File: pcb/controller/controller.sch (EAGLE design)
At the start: 86 parts, among them J1 DL-2MM-HEADER-14, J10 SNG-100-HEADER-03-HDR-V, J2 DL-1.25MM-HEADER-20, J3 MICRO_SD, J4 SNG-2MM-HEADER-03-SMT-V, J5 7498011122R, J6 USB_A, J7 SNG-2MM-HEADER-09-V, J8 CUI-PJ-013C, J9 SNG-100-HEADER-04-HDR-V, Q1 12MHz, U1 LM3526M-L, U2 ARIA_G25, U3 PCM2704C, U4 TPA2005D1DGN, U5 ADP2303ARDZ, U6 TPS62086RLT, U7 TS4040D30IDBZ

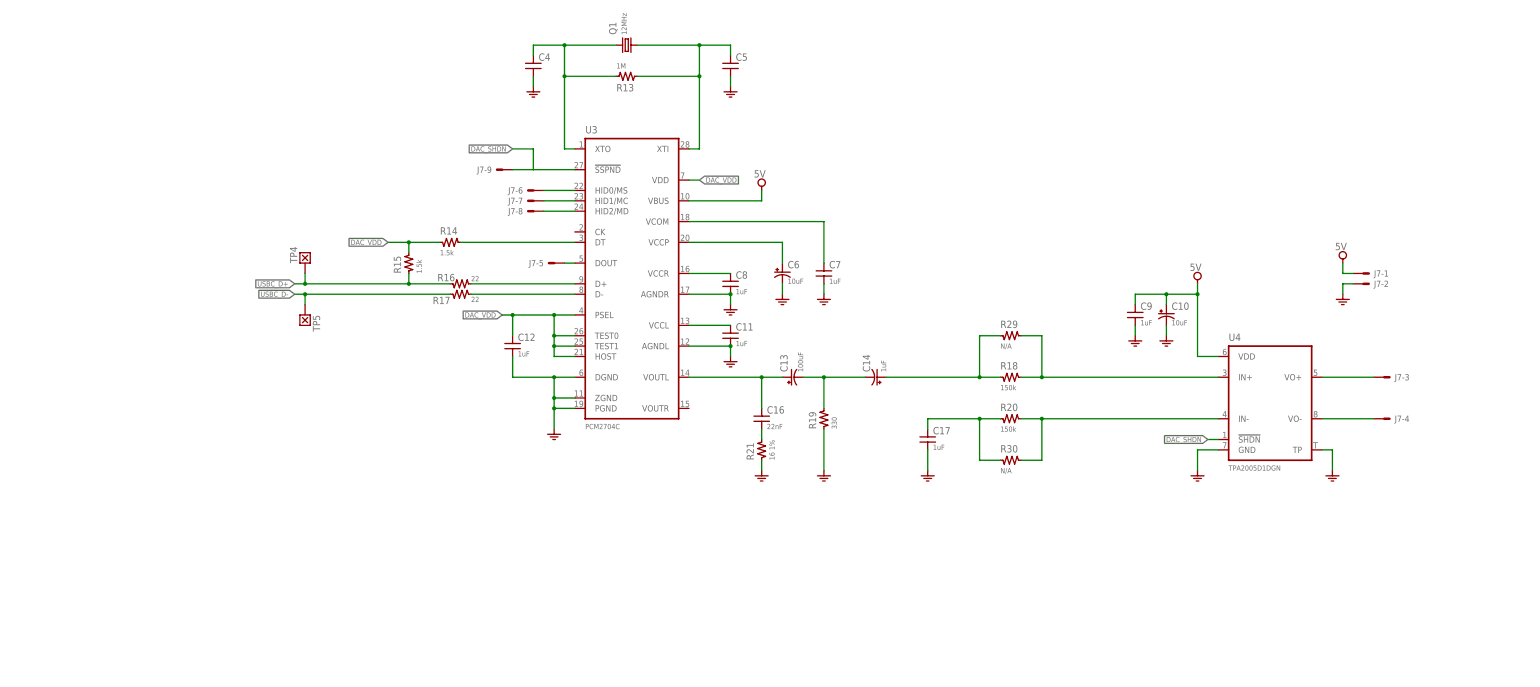
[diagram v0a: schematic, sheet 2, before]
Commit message: Corrected drawings of touch panel PCB
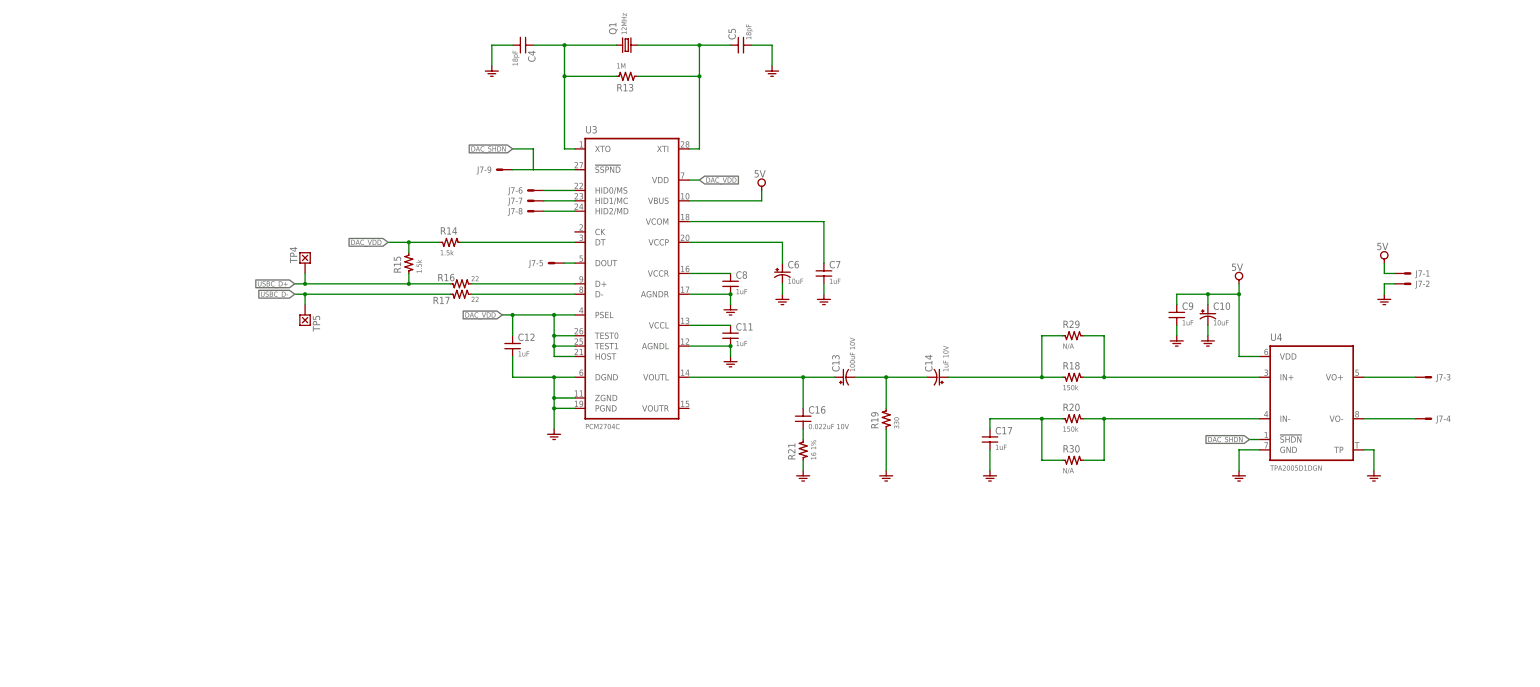
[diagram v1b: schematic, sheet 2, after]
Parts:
- removed R22, R27: 100k, Passive:RES-0603
- removed R23: 53.6K 1%, Passive:RES-0603
- removed R25: 10K 1%, Passive:RES-0603
- added C15: 10uF 10v, Passive:CAP-1206
- added C27: 22uF 6.3V, Passive:CAP-1206
- added C28: 47uF 6.3v, Passive:CAP-1206
- added D2: 30V 4A, Passive:DIODE-DO214-AA
- C13: value 100uF -> 100uF 10V
- C14: value 1uF -> 1uF 10V
- C16: value 22nF -> 0.022uF 10V
- C18, C19: value 10uF 50V -> 10uF 25V; device Passive:CAP-0805 -> Passive:CAP-1206; DESCRIPTION {DESCRIPTION} - SMT 0805 - {value} -> {DESCRIPTION} - SMT 1206 - {value}; PACKAGE SMT 0805 -> SMT 1206
- C21: value 100nF -> 100nF 25v
- C22: value 10uF 50v -> 10uF 25v
- C23: value 100uF -> 22uF 6.3V
- C24: value (none) -> 100nF; device Passive:CAP-1206 -> Passive:CAP-0603
- C25: value (none) -> 47uF 6.3v
- C26: value (none) -> 100nF
- C4, C5: value (none) -> 18pF
- D1: value 40V 3A -> 30V 4A
- L4: value (none) -> 10uH; device Passive:IND-74437324022 -> Passive:IND-10X10; MFG (none) -> TDK; PART_NO (none) -> CLF10040T-100M
- L5: value (none) -> 4.7uH; device Passive:IND-MPI4040R2-R47-R -> Passive:IND-10X10; PART_NO (none) -> CLF10040T-4R7N
- TP1, TP2: device Misc:TEST_POINT-050 -> Misc:WIRE
- U5: value ADP2303ARDZ -> ADP2302ARDZ-5.0; device Power:ADP2303ARDZ -> Power:ADP2302ARDZ-5.0; DESCRIPTION (none) -> {DESCRIPTION} - 2A, 5V
- U6: value TPS62086RLT -> ADP2303ARDZ-3.3; device Power:TPS62086RLT -> Power:ADP2303ARDZ-3.3; DESCRIPTION (none) -> {DESCRIPTION} - 3A, 3.3v
- U7: value TS4040D30IDBZ -> LM4040D25IDBZR; PART_NO (none) -> LM4040D25IDBZR
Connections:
- net N$2 renamed IN_GND
- removed net N$3: R22.2, U5.PGOOD
- removed net N$34: R23.1, R25.2, U5.FB
- removed net N$35: L5.P$1, U6.SW
- new net N$10: C24.2, D2.K, L5.1, U6.SW
- net 3.3V: now also C28.1, L5.2; no longer L5.P$2, R27.2, U6.VOS
- net 5V: now also C27.1, L4.2, U5.FB; no longer C24.1, L4.P$2, R23.2, U6.EN, U6.VIN
- net GND: now also C15.2, C27.2, C28.2, D2.A, U6.EPAD, U6.GND; no longer C24.2, R25.1
- net N$33: now also L4.1; no longer L4.P$1
- net N$36: now also C24.1, U6.BST; no longer R27.1, U6.PG
- net VCC: now also C15.1, J9-1.S, U6.EN, U6.VIN; no longer J9-2.S, R22.1
- net V_MAIN: now also J9-2.S; no longer J9-1.S
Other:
- note added: "3.3V STEP DOWN DC-DC"
- moved on the sheet: C10, C13, C14, C16, C17, C22, C23, C24, C25, C4, C5, C9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

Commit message: Display base pcb (rev C), Touch panel (rev B)
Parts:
- removed J10: SNG-100-HEADER-03-HDR-V, Connectors:SNG-100-HEADER-03-HDR-V
- removed R17: 22, Passive:RES-0603
- removed TP3: (no value), Misc:TEST_POINT-TP_75X75
- removed TP4, TP5: (no value), Misc:TEST_POINT-050
- added C29: 1uF, Passive:CAP-0603
- added C30: 22uF (10v), Passive:CAP-E-1206-TANT
- added C31: 47uF (6.3v), Passive:CAP-E-1206-TANT
- added C32, C33: N/A, Passive:CAP-0603
- added L6, L7: 0, Passive:IND-0603
- added R22, R23: 1 (1%), Passive:RES-0805
- added U8: CAT811TTBI, IC:CAT811TTBI
- added W1: (no value), Misc:WIRE-150X75
- added W2: DRX, Misc:WIRE-150X75
- added W3: DTX, Misc:WIRE-150X75
- added W4: GND, Misc:WIRE-150X75
- C10, C14, C6: device Passive:CAP-E-S0805 -> Passive:CAP-E-0805-ALUM; DESCRIPTION (none) -> Aluminium capacitor - SMT 0805 - {VALUE}
- C13: device Passive:CAP-E-S1210 -> Passive:CAP-E-1210-ALUM; DESCRIPTION (none) -> Aluminium capacitor - SMT 1210 - {VALUE}; MFG (none) -> AVX
- C15: value 10uF 10v -> 10uF (25v); device Passive:CAP-1206 -> Passive:CAP-E-1210-TANT; DESCRIPTION {DESCRIPTION} - SMT 1206 - {value} -> (none); MFG (none) -> AVX; PACKAGE SMT 1206 -> (none); PART_NO (none) -> TPSB106K025R1800
- C21: value 100nF 25v -> 100nF 25V
- C22: value 10uF 25v -> 10uF (25v); device Passive:CAP-1206 -> Passive:CAP-E-1210-TANT; DESCRIPTION {DESCRIPTION} - SMT 1206 - {value} -> (none); MFG (none) -> AVX; PACKAGE SMT 1206 -> (none); PART_NO (none) -> TPSB106K025R1800
- C23: value 22uF 6.3V -> 22uF (10v); device Passive:CAP-1206 -> Passive:CAP-E-1206-TANT; DESCRIPTION (none) -> Tantalum capacitor - SMT 1206 - {VALUE}; MFG (none) -> AVX; PART_NO (none) -> TPSA226M010R0900
- C24: value 100nF -> 100nF 25V
- C25: value 47uF 6.3v -> 47uF (6.3v); device Passive:CAP-1206 -> Passive:CAP-E-1206-TANT; DESCRIPTION (none) -> Tantalum capacitor - SMT 1206 - {VALUE}; MFG (none) -> AVX; PART_NO (none) -> TPSA476K006R0800
- C27: value 22uF 6.3V -> 1nF; device Passive:CAP-1206 -> Passive:CAP-0805; DESCRIPTION {DESCRIPTION} - SMT 1206 - {value} -> (none); PACKAGE SMT 1206 -> (none)
- C28: value 47uF 6.3v -> 1nF; device Passive:CAP-1206 -> Passive:CAP-0805; DESCRIPTION {DESCRIPTION} - SMT 1206 - {value} -> {DESCRIPTION} - SMT 0805 - {value}; PACKAGE SMT 1206 -> SMT 0805
- D1: value 30V 4A -> 30V 2A
- J1: value DL-2MM-HEADER-14 -> SNG-2MM-HEADER-04-V; device Connectors:DL-2MM-HEADER-14 -> Connectors:SNG-2MM-HEADER-04-V; DESCRIPTION (none) -> {DESCRIPTION} - Vertical; SKU (none) -> DF3A-4P-2DSA
- J4: value SNG-2MM-HEADER-03-SMT-V -> SNG-100-HEADER-01-HDR-V; device Connectors:SNG-2MM-HEADER-03-SMT-V -> Connectors:SNG-100-HEADER-01-HDR-V; SKU DF3DZ-3P-2VXX -> (none)
- J7: value SNG-2MM-HEADER-09-V -> DL-1.25MM-HEADER-10; device Connectors:SNG-2MM-HEADER-09-V -> Connectors:DL-1.25MM-HEADER-10
- J9: value SNG-100-HEADER-04-HDR-V -> SNG-100-HEADER-05-HDR-V; device Connectors:SNG-100-HEADER-04-HDR-V -> Connectors:SNG-100-HEADER-05-HDR-V
- L4: value 10uH -> 22uH
- L5: value 4.7uH -> 22uH
- Q1: device Crystal:XTALHC49S -> Crystal:XTALHC49UP
- R1: value 10k -> 22
- R16: value 22 -> 2.2k
- R2: value 10k -> 22; DESCRIPTION {DESCRIPTION} - SMT 0603 - {VALUE} -> (none); PACKAGE SMT 0603 -> (none)
- R21: value 16 1% -> 16 (1%)
- R24: value 12M 1% -> 12M (1%)
- R26: value 4.7M 1% -> 4.7M (1%)
- TP1, TP2: device Misc:WIRE -> Misc:WIRE-150X75
- U3: value PCM2704C -> PCM2704CDB; device IC:PCM2704C -> IC:PCM2704CDB
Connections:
- net N$21 renamed HID1
- net N$23 renamed VOUTL
- removed net !RESET: J1-10.S, U2.NRST
- removed net 1WIRE: U2.PA21/1WIRE
- removed net AD2: J2-13.S, U2.PB13/AD2
- removed net AD3: J2-15.S, U2.PB14/AD3
- removed net EXP_MISO: J1-6.S, U2.PA14/MISO
- removed net EXP_MOSI: J1-8.S, U2.PA13/MOSI
- removed net EXP_NPCS0: J1-5.S, U2.PA11/NPCS0
- removed net EXP_SPCK: J1-7.S, U2.PA12/SPCK
- removed net N$10: C24.2, D2.K, L5.1, U6.SW
- removed net N$22: J7-8.S, U3.HID2/MD
- removed net N$30: J7-5.S, U3.DOUT
- removed net N$33: C21.2, D1.K, L4.1, U5.SW
- removed net PA0: J2-6.S, U2.PA0/TXD0
- removed net PA1: J2-8.S, U2.PA1/RXD0
- removed net PA2: J2-10.S, U2.PA2/RTS0
- removed net PA23: U2.PA23
- removed net PA24: U2.PA24
- removed net PA25: U2.PA25
- removed net PA3: J2-12.S, U2.PA3/CTS0
- removed net PA4: J2-14.S, U2.PA4
- removed net PA5: J2-16.S, U2.PA5/TXD1
- removed net PA6: J2-18.S, U2.PA6/RXD1
- removed net PA7: J2-20.S, U2.PA7/TXD2
- removed net PA8: U2.PA8/RXD2
- removed net PC17: U2.PC17/URXD1
- removed net PWM0: U2.PC18/PWM0
- removed net PWM1: J2-17.S, U2.PC19/PWM1
- removed net PWM2: J2-19.S, U2.PC20/PWM2
- removed net PWM3: J1-4.S, U2.PC21/PWM3
- removed net SCL1: J1-3.S, R4.2, U2.PC1/SCL1
- removed net SDA1: J1-1.S, R3.2, U2.PC0/SDA1
- new net DOUT: J7-1.S, U3.DOUT
- new net HID0: J7-5.S, U3.HID0/MS
- new net HID2: J7-3.S, U3.HID2/MD
- new net MISO: J2-20.S, U2.PA14/MISO
- new net MOSI: J2-18.S, U2.PA13/MOSI
- new net N$2: C27.1, R22.1
- new net N$21: R16.1, U8.!RST
- new net N$3: C28.1, R23.1
- new net NRST: R16.2, U2.NRST
- new net PC18/PWM0: J2-10.S, U2.PC18/PWM0
- new net PC19/PWM1: J2-12.S, U2.PC19/PWM1
- new net PC22/TXD3: J2-13.S, U2.PC22/TXD3
- new net PC23/RXD3: J2-15.S, U2.PC23/RXD3
- new net PC24/RTS3: J2-17.S, U2.PC24/RTS3
- new net PC25/CTS3: J2-19.S, U2.PC25/CTS3
- new net SPCK: J2-16.S, U2.PA12/SPCK
- new net SPI_CS0: J2-14.S, U2.PA11/NPCS0
- new net SPK+: C33.1, J7-10.S, L6.2
- new net SPK-: C32.1, J7-9.S, L7.2
- new net SW_3.3: C24.2, D2.K, L5.1, R23.2, U6.SW
- new net SW_5V: C21.2, D1.K, L4.1, R22.2, U5.SW
- net 3.3V: now also C25.+, C31.+, J2-7.S, J2-9.S, U8.VCC; no longer C25.1, C28.1, J1-9.S, J2-2.S, J2-4.S, R1.1, R2.1
- net 5V: now also C23.+, C29.1, C30.+, J2-2.S, J2-4.S, J7-8.S; no longer C23.1, C27.1, J10-2.S, J2-1.S, J7-1.S
- net DAC_SHDN: now also J7-4.S; no longer J7-9.S
- net DRX: now also W2.P$1; no longer J4-1.S
- net DTX: now also W3.P$1; no longer J4-3.S
- net GND: now also C15.-, C22.-, C23.-, C25.-, C29.2, C30.-, C31.-, C32.2, C33.2, J1-4.S, J2-1.S, J4.S, J7-6.S, U2.GND@7, U8.GND, W4.P$1; no longer C15.2, C22.2, C23.2, C25.2, J1-12.S, J1-14.S, J10-1.S, J4-2.S, J7-2.S, TP3.P$1
- net N$12: now also R2.2; no longer R16.2
- net N$13: now also R1.2; no longer R17.2
- net N$15: now also C6.+; no longer C7.1
- net N$16: now also C7.1; no longer C6.+
- net N$20: now also U3.VOUTR, W1.P$1; no longer J7-6.S, U3.HID0/MS
- net N$24: now also L6.1; no longer J7-3.S
- net N$25: now also L7.1; no longer J7-4.S
- net SCL0: now also J2-8.S, R4.2; no longer J2-9.S, R2.2
- net SDA0: now also J2-6.S, R3.2; no longer J2-7.S, R1.2
- net USBB_5V: now also J1-1.S; no longer J1-2.S
- net USBB_D+: now also R15.1, R2.1; no longer J1-13.S
- net USBB_D-: now also R1.1; no longer J1-11.S
- net USBC_D+: now also J1-3.S; no longer R15.1, R16.1, TP4.P$1
- net USBC_D-: now also J1-2.S; no longer R17.1, TP5.P$1
- net VCC: now also C15.+, C22.+, J9-5.S; no longer C15.1, C22.1, J9-1.S
- net V_AUX_MON: now also J9-2.S; no longer J10-3.S
- net V_AUX_ON: now also J9-1.S; no longer J9-4.S
- net V_MAIN: now also J9-4.S; no longer J9-2.S
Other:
- note added: "3.3V STEP DOWN REGULATOR"
- note added: "5V STEP DOWN REGULATOR"
- note removed: "3.3V STEP DOWN DC-DC"
- note removed: "5V STEP DOWN DC-DC"
- moved on the sheet: C21, C24, C27, C28, C6, C7, D1, D2, J1-1, J1-2, J1-3, J1-4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

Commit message: Changed page format on schematics to US letter (8.5" x 11")
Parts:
- added R17: (no value), Passive:RES-1206
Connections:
- new net 5V_AUD: C10.+, C29.1, C9.1, J7-8.S, R17.2, U3.VBUS, U4.VDD
- net 5V: now also R17.1; no longer C10.+, C29.1, C9.1, J7-8.S, U3.VBUS, U4.VDD
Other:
- note added: "PSU SUPERVISOR"

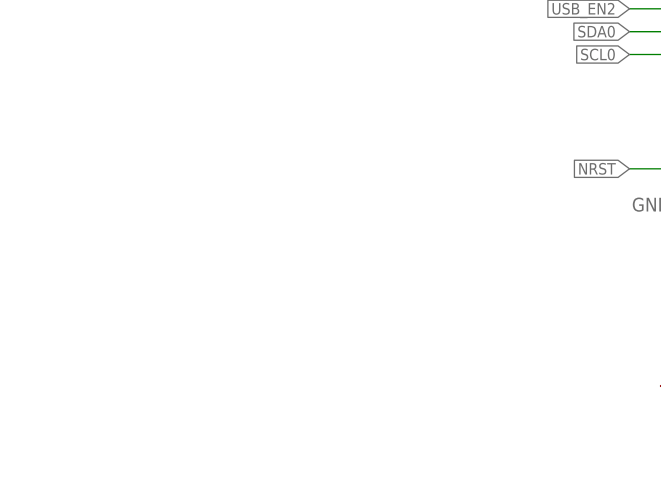
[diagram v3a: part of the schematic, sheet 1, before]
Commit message: Added a temperature sensor IC (U9) to controller PCB
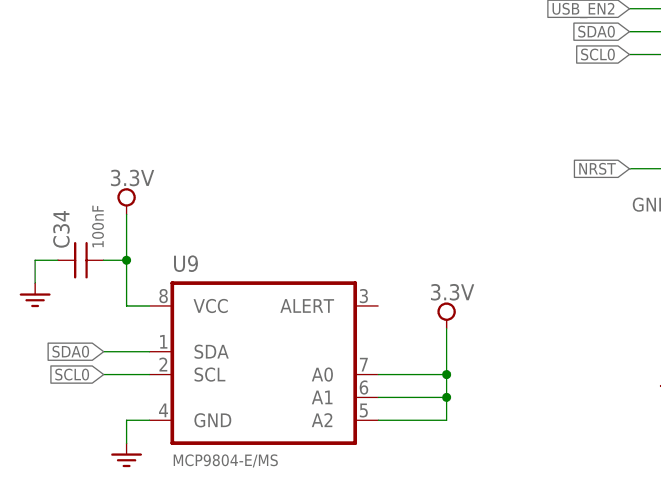
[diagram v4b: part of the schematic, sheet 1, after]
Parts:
- added C34: 100nF, Passive:CAP-0603
- added U9: MCP9804-E/MS, IC:MCP9804-E/MS
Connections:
- net VCC renamed V_IN
- net 3.3V: now also C34.2, U9.A0, U9.A1, U9.A2, U9.VCC
- net GND: now also C34.1, U9.GND
- net SCL0: now also U9.SCL
- net SDA0: now also U9.SDA
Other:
- moved on the sheet: J1-1, J1-2, J1-3, J1-4
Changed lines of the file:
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@@
 <part name="R17" library="Passive" deviceset="RES" device="-1206"/>
 <part name="FRAME4" library="Symbols" deviceset="FRAME_LETTER" device=""/>
+<part name="U9" library="IC" deviceset="MCP9804-*/?" device="MS" technology="E"/>
+<part name="GND32" library="Power" deviceset="GND" device=""/>
+<part name="SUPPLY5" library="Power" deviceset="3.3V" device=""/>
+<part name="SUPPLY6" library="Power" deviceset="3.3V" device=""/>
+<part name="C34" library="Passive" deviceset="CAP" device="-0603" value="100nF"/>
+<part name="GND51" library="Power" deviceset="GND" device=""/>
 </parts>
 <sheets>
@@
 <instance part="W3" gate="G$1" x="58.42" y="119.38" rot="R180"/>
 <instance part="W4" gate="G$1" x="58.42" y="116.84" rot="R180"/>
+<instance part="U9" gate="G$1" x="40.64" y="25.4"/>
+<instance part="GND32" gate="GND" x="25.4" y="15.24"/>
+<instance part="SUPPLY5" gate="1.8V" x="25.4" y="45.72"/>
+<instance part="SUPPLY6" gate="1.8V" x="60.96" y="33.02"/>
+<instance part="C34" gate="A" x="20.32" y="38.1" rot="R90"/>
+<instance part="GND51" gate="GND" x="15.24" y="33.02"/>
 </instances>
 <busses>
@@
 <junction x="200.66" y="170.18"/>
 </segment>
+<segment>
+<pinref part="U9" gate="G$1" pin="GND"/>
+<pinref part="GND32" gate="GND" pin="GND"/>
+<wire x1="27.94" y1="20.32" x2="25.4" y2="20.32" width="0.1524" layer="91"/>
+<wire x1="25.4" y1="20.32" x2="25.4" y2="17.78" width="0.1524" layer="91"/>
+</segment>
+<segment>
+<pinref part="C34" gate="A" pin="1"/>
+<pinref part="GND51" gate="GND" pin="GND"/>
+<wire x1="17.78" y1="38.1" x2="15.24" y2="38.1" width="0.1524" layer="91"/>
+<wire x1="15.24" y1="38.1" x2="15.24" y2="35.56" width="0.1524" layer="91"/>
+</segment>
 </net>
 <net name="EARTH" class="0">
@@
 <junction x="195.58" y="165.1"/>
 </segment>
+<segment>
+<pinref part="SUPPLY5" gate="1.8V" pin="3.3V"/>
+<wire x1="25.4" y1="43.18" x2="25.4" y2="38.1" width="0.1524" layer="91"/>
+<pinref part="U9" gate="G$1" pin="VCC"/>
+<wire x1="25.4" y1="38.1" x2="25.4" y2="33.02" width="0.1524" layer="91"/>
+<wire x1="25.4" y1="33.02" x2="27.94" y2="33.02" width="0.1524" layer="91"/>
+<pinref part="C34" gate="A" pin="2"/>
+<wire x1="22.86" y1="38.1" x2="25.4" y2="38.1" width="0.1524" layer="91"/>
+<junction x="25.4" y="38.1"/>
+</segment>
+<segment>
+<pinref part="SUPPLY6" gate="1.8V" pin="3.3V"/>
+<wire x1="60.96" y1="30.48" x2="60.96" y2="25.4" width="0.1524" layer="91"/>
+<pinref part="U9" gate="G$1" pin="A0"/>
+<wire x1="60.96" y1="25.4" x2="53.34" y2="25.4" width="0.1524" layer="91"/>
+<wire x1="60.96" y1="25.4" x2="60.96" y2="22.86" width="0.1524" layer="91"/>
+<junction x="60.96" y="25.4"/>
+<pinref part="U9" gate="G$1" pin="A1"/>
+<wire x1="60.96" y1="22.86" x2="53.34" y2="22.86" width="0.1524" layer="91"/>
+<pinref part="U9" gate="G$1" pin="A2"/>
+<wire x1="53.34" y1="20.32" x2="60.96" y2="20.32" width="0.1524" layer="91"/>
+<wire x1="60.96" y1="20.32" x2="60.96" y2="22.86" width="0.1524" layer="91"/>
+<junction x="60.96" y="22.86"/>
+</segment>
 </net>
 <net name="ETH_LINK" class="0">
@@
 <label x="30.48" y="165.1" size="1.27" layer="95" xref="yes"/>
 </segment>
+<segment>
+<pinref part="U9" gate="G$1" pin="SDA"/>
+<wire x1="27.94" y1="27.94" x2="22.86" y2="27.94" width="0.1524" layer="91"/>
+<label x="22.86" y="27.94" size="1.27" layer="95" rot="R180" xref="yes"/>
+</segment>
 </net>
 <net name="SCL0" class="0">
@@
 <wire x1="25.4" y1="157.48" x2="30.48" y2="157.48" width="0.1524" layer="91"/>
 <label x="30.48" y="157.48" size="1.27" layer="95" xref="yes"/>
+</segment>
+<segment>
+<pinref part="U9" gate="G$1" pin="SCL"/>
+<wire x1="27.94" y1="25.4" x2="22.86" y2="25.4" width="0.1524" layer="91"/>
+<label x="22.86" y="25.4" size="1.27" layer="95" rot="R180" xref="yes"/>
 </segment>
 </net>
@@
 </segment>
 </net>
-<net name="VCC" class="0">
+<net name="V_IN" class="0">
 <segment>
 <pinref part="J9" gate="-5" pin="S"/>
@@
 <instance part="R11" gate="A" x="63.5" y="91.44" rot="R90"/>
 <instance part="GND10" gate="GND" x="68.58" y="81.28"/>
-<instance part="J1" gate="-1" x="149.86" y="96.52"/>
-<instance part="J1" gate="-2" x="149.86" y="93.98"/>
-<instance part="J1" gate="-3" x="149.86" y="91.44"/>
-<instance part="J1" gate="-4" x="149.86" y="88.9"/>
-<instance part="GND11" gate="GND" x="144.78" y="83.82"/>
+<instance part="J1" gate="-1" x="160.02" y="96.52"/>
+<instance part="J1" gate="-2" x="160.02" y="93.98"/>
+<instance part="J1" gate="-3" x="160.02" y="91.44"/>
+<instance part="J1" gate="-4" x="160.02" y="88.9"/>
+<instance part="GND11" gate="GND" x="154.94" y="83.82"/>
 </instances>
 <busses>
@@
 <pinref part="J1" gate="-4" pin="S"/>
 <pinref part="GND11" gate="GND" pin="GND"/>
-<wire x1="147.32" y1="88.9" x2="144.78" y2="88.9" width="0.1524" layer="91"/>
-<wire x1="144.78" y1="88.9" x2="144.78" y2="86.36" width="0.1524" layer="91"/>
+<wire x1="157.48" y1="88.9" x2="154.94" y2="88.9" width="0.1524" layer="91"/>
+<wire x1="154.94" y1="88.9" x2="154.94" y2="86.36" width="0.1524" layer="91"/>
 </segment>
 </net>
@@
 <segment>
 <pinref part="J1" gate="-1" pin="S"/>
-<wire x1="147.32" y1="96.52" x2="139.7" y2="96.52" width="0.1524" layer="91"/>
-<label x="139.7" y="96.52" size="1.27" layer="95" rot="R180" xref="yes"/>
+<wire x1="157.48" y1="96.52" x2="149.86" y2="96.52" width="0.1524" layer="91"/>
+<label x="149.86" y="96.52" size="1.27" layer="95" rot="R180" xref="yes"/>
 </segment>
 </net>
@@
 <segment>
 <pinref part="J1" gate="-2" pin="S"/>
-<wire x1="147.32" y1="93.98" x2="139.7" y2="93.98" width="0.1524" layer="91"/>
-<label x="139.7" y="93.98" size="1.27" layer="95" rot="R180" xref="yes"/>
+<wire x1="157.48" y1="93.98" x2="149.86" y2="93.98" width="0.1524" layer="91"/>
+<label x="149.86" y="93.98" size="1.27" layer="95" rot="R180" xref="yes"/>
 </segment>
 </net>
@@
 <segment>
 <pinref part="J1" gate="-3" pin="S"/>
-<wire x1="147.32" y1="91.44" x2="139.7" y2="91.44" width="0.1524" layer="91"/>
-<label x="139.7" y="91.44" size="1.27" layer="95" rot="R180" xref="yes"/>
-</segment>
-</net>
+<wire x1="157.48" y1="91.44" x2="149.86" y2="91.44" width="0.1524" layer="91"/>
+<label x="149.86" y="91.44" size="1.27" layer="95" rot="R180" xref="yes"/>
+</segment>
+</net>
